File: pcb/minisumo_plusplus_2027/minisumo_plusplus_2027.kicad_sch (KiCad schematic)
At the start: 9 parts, among them J1 IR - Conn_01x03_Pin, J2 IR - Conn_01x03_Pin, J3 Start Module - Conn_01x04_Pin, J4 US - Conn_01x04_Pin, SW1 SW_SPDT, U3 ESP32-C6-SuperMini

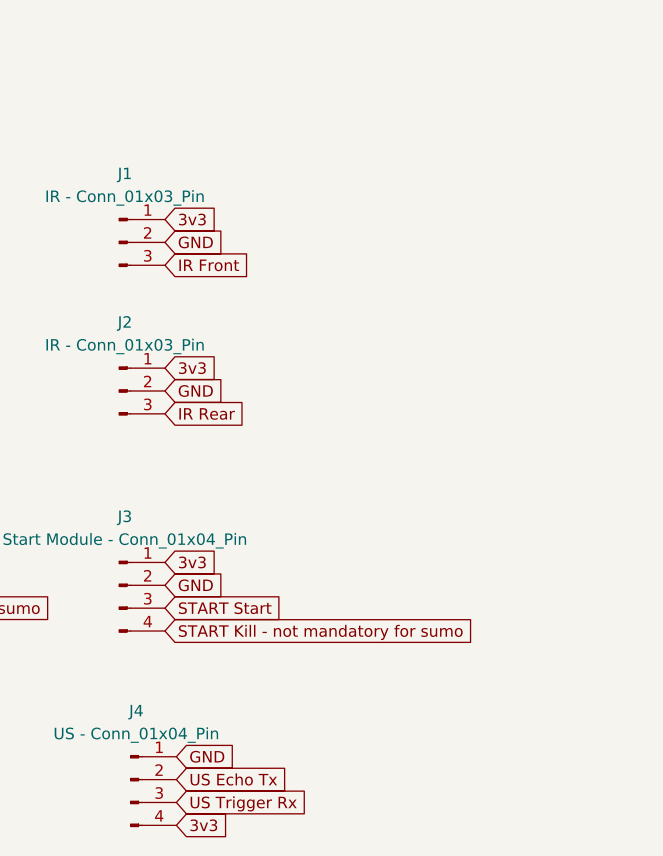
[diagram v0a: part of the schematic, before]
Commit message: pcb - 1x10 for ir front/back and ultrasonic instead of 2x 1x3 + 1x4 && also included a 6x fab board example of latest board
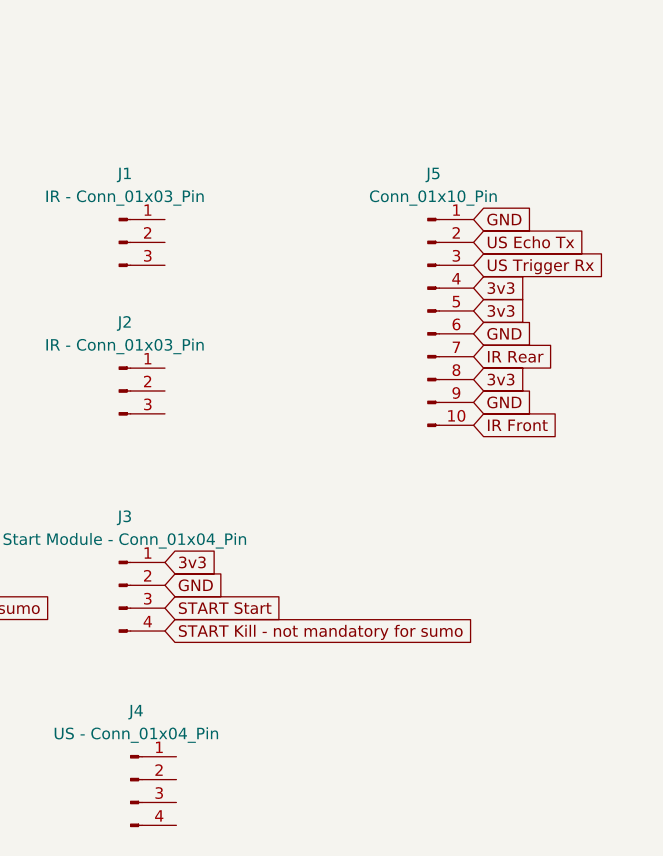
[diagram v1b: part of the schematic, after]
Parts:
- added J5: Conn_01x10_Pin, Connector_PinHeader_2.54mm:PinHeader_1x10_P2.54mm_Vertical, symbol Connector:Conn_01x10_Pin
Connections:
- net 3v3: now also J5.4 (Pin_4), J5.5 (Pin_5), J5.8 (Pin_8); no longer J1.1 (Pin_1), J2.1 (Pin_1), J4.4 (Pin_4)
- net GND: now also J5.1 (Pin_1), J5.6 (Pin_6), J5.9 (Pin_9); no longer J1.2 (Pin_2), J2.2 (Pin_2), J4.1 (Pin_1)
- net IR Front: now also J5.10 (Pin_10); no longer J1.3 (Pin_3)
- net IR Rear: now also J5.7 (Pin_7); no longer J2.3 (Pin_3)
- net US Echo Tx: now also J5.2 (Pin_2); no longer J4.2 (Pin_2)
- net US Trigger Rx: now also J5.3 (Pin_3); no longer J4.3 (Pin_3)

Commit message: pcb now with 2a buck boost MT3608, updated footprints incl motor driver @2.54 pins int1-4, and c6 && 3d with updated buck boost along with pcb!
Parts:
- added A3: (no value), minisumo_plusplus_2027:MT3608 DC-DC Boost Module – 28V 2A Step-Up Power Module, symbol minisumo_plusplus_2027:XL6009_4A_Boost_Converter_Step_Up_Adjustable_15W_5-32V_t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
- A1: footprint (none) -> minisumo_plusplus_2027:Mini_L298N_2_Channel_H_Bridge_DC_Motor_Driver_Board_with_MX1508-2.54_int1-4-special_silk
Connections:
- net 3v7 (>3v3 & <5v): now also A3.1 (IN+)
- net 9v: now also A3.3 (OUT+)
- net GND: now also A3.2 (IN-)
- net at A1.2 (gnd), A2.4 (OUT-): now also A3.4 (OUT-)
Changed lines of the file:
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@@
+	)
+	(junction
+		(at 74.93 58.42)
+		(diameter 0)
+		(color 0 0 0 0)
 	)
 	(junction
@@
 		(color 0 0 0 0)
 	)
+	(junction
+		(at 50.8 53.34)
+		(diameter 0)
+		(color 0 0 0 0)
+	)
+	(junction
+		(at 72.39 53.34)
+		(diameter 0)
+		(color 0 0 0 0)
+	)
+	(junction
+		(at 48.26 58.42)
+		(diameter 0)
+		(color 0 0 0 0)
+	)
 	(wire
 		(pts
@@
 	(wire
 		(pts
+			(xy 72.39 53.34) (xy 121.92 53.34)
+		)
+		(stroke
+			(width 0)
+			(type default)
+		)
+	)
+	(wire
+		(pts
 			(xy 111.76 58.42) (xy 111.76 46.99)
 		)
@@
 	(wire
 		(pts
-			(xy 69.85 53.34) (xy 121.92 53.34)
+			(xy 69.85 53.34) (xy 72.39 53.34)
 		)
 		(stroke
@@
 	(wire
 		(pts
+			(xy 48.26 58.42) (xy 48.26 76.2)
+		)
+		(stroke
+			(width 0)
+			(type default)
+		)
+	)
+	(wire
+		(pts
+			(xy 74.93 58.42) (xy 111.76 58.42)
+		)
+		(stroke
+			(width 0)
+			(type default)
+		)
+	)
+	(wire
+		(pts
 			(xy 49.53 63.5) (xy 40.64 63.5)
 		)
@@
 	(wire
 		(pts
+			(xy 48.26 76.2) (xy 52.07 76.2)
+		)
+		(stroke
+			(width 0)
+			(type default)
+		)
+	)
+	(wire
+		(pts
 			(xy 115.57 102.87) (xy 123.19 102.87)
 		)
@@
 	(wire
 		(pts
+			(xy 50.8 53.34) (xy 50.8 71.12)
+		)
+		(stroke
+			(width 0)
+			(type default)
+		)
+	)
+	(wire
+		(pts
 			(xy 41.91 72.39) (xy 41.91 118.11)
 		)
@@
 	(wire
 		(pts
-			(xy 40.64 58.42) (xy 52.07 58.42)
+			(xy 52.07 71.12) (xy 50.8 71.12)
+		)
+		(stroke
+			(width 0)
+			(type default)
+		)
+	)
+	(wire
+		(pts
+			(xy 40.64 58.42) (xy 48.26 58.42)
+		)
+		(stroke
+			(width 0)
+			(type default)
+		)
+	)
+	(wire
+		(pts
+			(xy 72.39 53.34) (xy 72.39 71.12)
 		)
 		(stroke
@@
 	(wire
 		(pts
-			(xy 68.58 58.42) (xy 111.76 58.42)
+			(xy 68.58 58.42) (xy 74.93 58.42)
+		)
+		(stroke
+			(width 0)
+			(type default)
+		)
+	)
+	(wire
+		(pts
+			(xy 48.26 58.42) (xy 52.07 58.42)
 		)
 		(stroke
@@
 	(wire
 		(pts
-			(xy 48.26 53.34) (xy 52.07 53.34)
+			(xy 48.26 53.34) (xy 50.8 53.34)
+		)
+		(stroke
+			(width 0)
+			(type default)
+		)
+	)
+	(wire
+		(pts
+			(xy 68.58 71.12) (xy 72.39 71.12)
 		)
 		(stroke
@@
 	(wire
 		(pts
+			(xy 50.8 53.34) (xy 52.07 53.34)
+		)
+		(stroke
+			(width 0)
+			(type default)
+		)
+	)
+	(wire
+		(pts
 			(xy 121.92 100.33) (xy 121.92 53.34)
 		)
@@
 	(wire
 		(pts
+			(xy 74.93 76.2) (xy 74.93 58.42)
+		)
+		(stroke
+			(width 0)
+			(type default)
+		)
+	)
+	(wire
+		(pts
 			(xy 69.85 46.99) (xy 69.85 53.34)
 		)
@@
 		(pts
 			(xy 46.99 66.04) (xy 46.99 113.03)
+		)
+		(stroke
+			(width 0)
+			(type default)
+		)
+	)
+	(wire
+		(pts
+			(xy 68.58 76.2) (xy 74.93 76.2)
 		)
 		(stroke
@@
 				(path "/65ad0d35-fb8f-4881-ae17-8c4840fba223"
 					(reference "U3")
+					(unit 1)
+				)
+			)
+		)
+	)
+	(symbol
+		(lib_id "minisumo_plusplus_2027:XL6009_4A_Boost_Converter_Step_Up_Adjustable_15W_5-32V_to_5-50V_DC-DC_Power_Supply_Module_LM2577_Step-up_Module")
+		(at 66.04 67.31 0)
+		(mirror y)
+		(unit 1)
+		(body_style 1)
+		(exclude_from_sim no)
+		(in_bom yes)
+		(on_board yes)
+		(in_pos_files yes)
+		(dnp no)
+		(fields_autoplaced yes)
+		(property "Reference" "A3"
+			(at 60.325 64.77 0)
+			(show_name no)
+			(do_not_autoplace no)
+			(effects
+				(font
+					(size 1.27 1.27)
+				)
+			)
+		)
+		(property "Value" ""
+			(at 66.04 67.31 0)
+			(show_name no)
+			(do_not_autoplace no)
+			(effects
+				(font
+					(size 1.27 1.27)
+				)
+			)
+		)
+		(property "Footprint" "minisumo_plusplus_2027:MT3608 DC-DC Boost Module – 28V 2A Step-Up Power Module"
+			(at 66.04 67.31 0)
+			(hide yes)
+			(show_name no)
+			(do_not_autoplace no)
+			(effects
+				(font
+					(size 1.27 1.27)
+				)
+			)
+		)
+		(property "Datasheet" "https://www.aliexpress.com/item/1005010504010086.html"
+			(at 66.04 67.31 0)
+			(hide yes)
+			(show_name no)
+			(do_not_autoplace no)
+			(effects
+				(font
+					(size 1.27 1.27)
+				)
+			)
+		)
+		(property "Description" "XL6009 4A Boost Converter Step Up Adjustable 15W 5-32V to 5-50V DC-DC Power Supply Module LM2577 Step-up Module"
+			(at 66.04 67.31 0)
+			(hide yes)
+			(show_name no)
+			(do_not_autoplace no)
+			(effects
+				(font
+					(size 1.27 1.27)
+				)
+			)
+		)
+		(pin "3"
+		)
+		(pin "1"
+		)
+		(pin "2"
+		)
+		(pin "4"
+		)
+		(instances
+			(project "minisumo_plusplus_2027"
+				(path "/65ad0d35-fb8f-4881-ae17-8c4840fba223"
+					(reference "A3")
 					(unit 1)
 				)
@@
 			)
 		)
-		(property "Footprint" ""
+		(property "Footprint" "minisumo_plusplus_2027:Mini_L298N_2_Channel_H_Bridge_DC_Motor_Driver_Board_with_MX1508-2.54_int1-4-special_silk"
 			(at 38.1 54.61 0)
 			(hide yes)

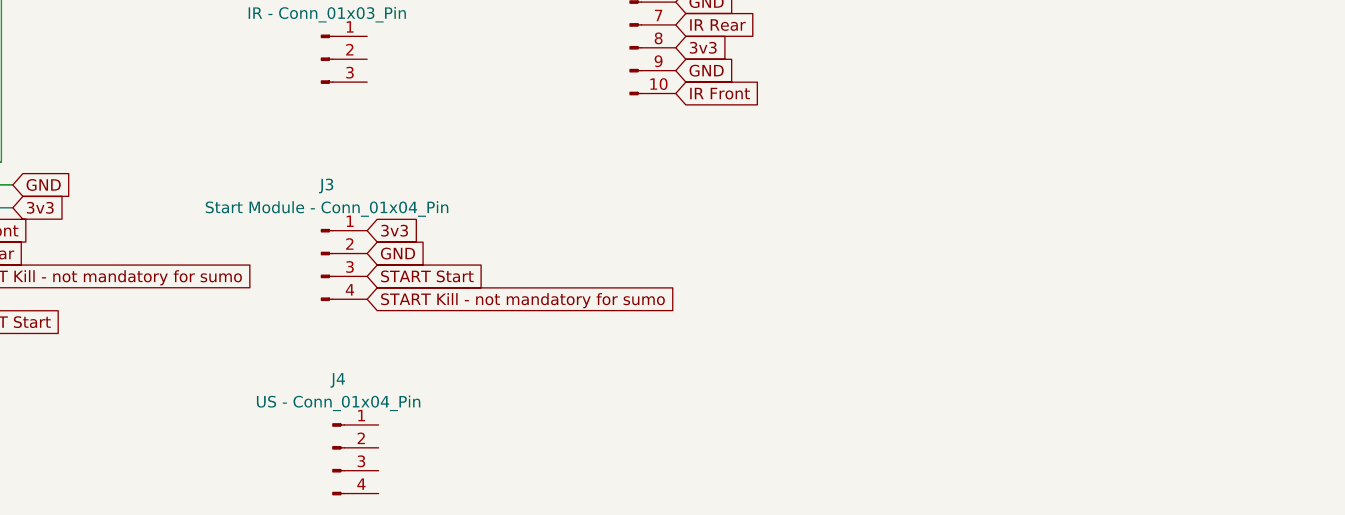
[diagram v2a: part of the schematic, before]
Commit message: pcb - updated footprints w 3d and fixed broken traces && 3d - redid assemblies they were a bit of a mess.
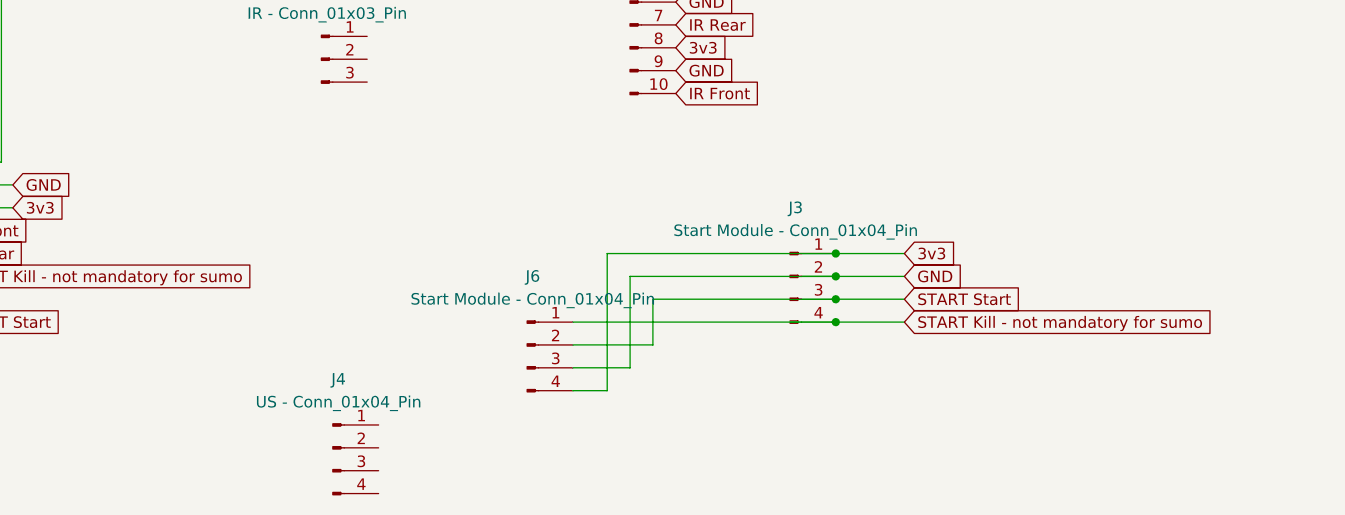
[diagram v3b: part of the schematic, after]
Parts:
- added J6: Start Module - Conn_01x04_Pin, Connector_PinSocket_2.54mm:PinSocket_1x04_P2.54mm_Horizontal, symbol Connector:Conn_01x04_Pin
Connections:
- net 3v3: now also J6.4 (Pin_4)
- net GND: now also J6.3 (Pin_3)
- net START Kill - not mandatory for sumo: now also J6.1 (Pin_1)
- net START Start: now also J6.2 (Pin_2)
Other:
- moved on the sheet: J3
